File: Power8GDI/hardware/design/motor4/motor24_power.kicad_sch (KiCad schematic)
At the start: 17 parts, among them Q6250 IPD90N10S4-06, Q6251 IPD90N10S4-06, U6250 LM74800QDRRRQ1

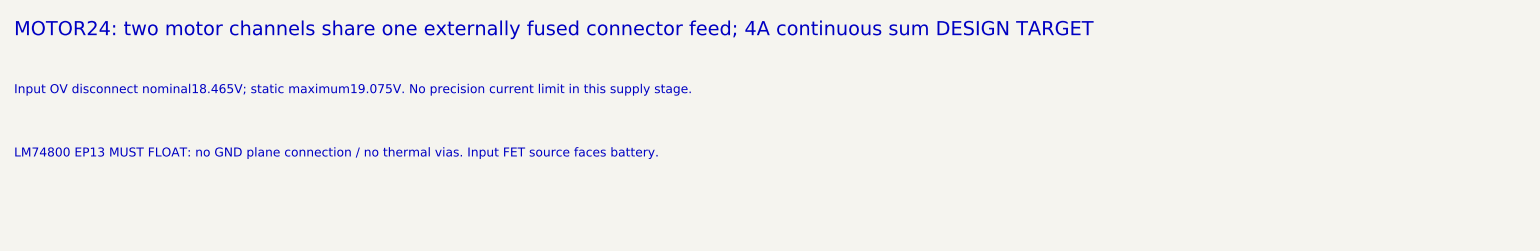
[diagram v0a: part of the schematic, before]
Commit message: Redesign sport target as six DI/PI channels with two motors and one lambda
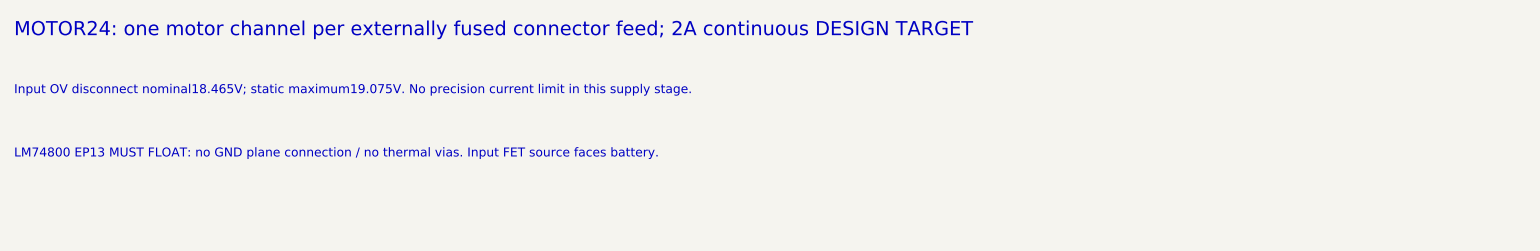
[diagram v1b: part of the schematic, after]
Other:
- note added: "MOTOR24: one motor channel per externally fused connector feed; 2A continuous DESIGN TARGET"
- note removed: "MOTOR24: two motor channels share one externally fused connector feed; 4A continuous sum DESIGN TARGET"
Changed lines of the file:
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@@
 (kicad_sch (version 20250114) (generator "eeschema") (paper "A2") (title_block (title "MOTOR24: independent protected feed") (rev "Engineering draft 0.1") (comment 1 "UNQUALIFIED: no manufacturing or engine approval"))
-(text "MOTOR24: two motor channels share one externally fused connector feed; 4A continuous sum DESIGN TARGET" (at 20 15 0) (effects (font (size 2 2)) (justify left top)))
+(text "MOTOR24: one motor channel per externally fused connector feed; 2A continuous DESIGN TARGET" (at 20 15 0) (effects (font (size 2 2)) (justify left top)))
 (text "Input OV disconnect nominal18.465V; static maximum19.075V. No precision current limit in this supply stage." (at 20 24 0) (effects (font (size 1.27 1.27)) (justify left top)))
 (text "LM74800 EP13 MUST FLOAT: no GND plane connection / no thermal vias. Input FET source faces battery." (at 20 33 0) (effects (font (size 1.27 1.27)) (justify left top)))

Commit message: Review B58 injector power stage and bind selected GDI6 BOM
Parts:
- C6250, C6251, C6252, C6253: Hardware_Qualification (none) -> BOARD_QUALIFICATION_PENDING; MPN (none) -> C0805C104K1RACTU; Manufacturer (none) -> KEMET; Procurement_Status (none) -> SELECTED_CATALOG_ITEM; Purchase_Released (none) -> false; Selection_Gaps (none) -> []; Selection_ID (none) -> SEL-50b208aec5b1; Selection_Ratings (none) -> {"capacitance_pf": 100000, "dielectric": "X7R", "rated_volt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; Selection_Source_URLs (none) -> https://www.mouser.com/datasheet/3/72/1/C0805C104K1RACTU.pdf
- C6254: Hardware_Qualification (none) -> BOARD_QUALIFICATION_PENDING; MPN (none) -> C0805C223K1RACTU; Manufacturer (none) -> KEMET; Procurement_Status (none) -> SELECTED_CATALOG_ITEM; Purchase_Released (none) -> false; Selection_Gaps (none) -> []; Selection_ID (none) -> SEL-514923e6d12b; Selection_Ratings (none) -> {"capacitance_pf": 22000, "dielectric": "X7R", "rated_volta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; Selection_Source_URLs (none) -> https://www.tme.com/Document/1eb495a6db632c9d0f71cb50aeea42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
- D6250: Hardware_Qualification (none) -> PINOUT_RATINGS_AND_DELIVERY_SUFFIX_REVIEW_PENDING; MPN (none) -> SMCJ33CA; Manufacturer (none) -> Littelfuse; Procurement_Status (none) -> REFERENCE_MPN_RETAINED; Purchase_Released (none) -> false; Selection_Gaps (none) -> ["Existing schematic MPN retained. Complete circuit rating/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; Selection_ID (none) -> SEL-57a5ac481027; Selection_Ratings (none) -> {}; Selection_Source_URLs (none) -> https://www.littelfuse.com/products/tvs-diodes/surface-moun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
- Q6250, Q6251: Hardware_Qualification (none) -> PINOUT_RATINGS_AND_DELIVERY_SUFFIX_REVIEW_PENDING; MPN (none) -> IPD90N10S406ATMA1; Manufacturer (none) -> Infineon Technologies; Procurement_Status (none) -> REFERENCE_MPN_RETAINED; Purchase_Released (none) -> false; Selection_Gaps (none) -> ["Existing schematic MPN retained. Complete circuit rating/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; Selection_ID (none) -> SEL-dc1735b932bf; Selection_Ratings (none) -> {}; Selection_Source_URLs (none) -> https://www.infineon.com/part/IPD90N10S4-06
- R6250: Hardware_Qualification (none) -> BOARD_QUALIFICATION_PENDING; MPN (none) -> RG2012P-1403-B-T5; Manufacturer (none) -> Susumu; Procurement_Status (none) -> SELECTED_CATALOG_ITEM; Purchase_Released (none) -> false; Selection_Gaps (none) -> []; Selection_ID (none) -> SEL-aca8c7a4773a; Selection_Ratings (none) -> {"aec_q200": true, "derating": "Use manufacturer power vers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; Selection_Source_URLs (none) -> https://www.digikey.com/en/products/detail/susumu/RG2012P-1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
- R6251: Hardware_Qualification (none) -> BOARD_QUALIFICATION_PENDING; MPN (none) -> RNCF0603BTE10K0; Manufacturer (none) -> Stackpole Electronics; Procurement_Status (none) -> SELECTED_CATALOG_ITEM; Purchase_Released (none) -> false; Selection_Gaps (none) -> []; Selection_ID (none) -> SEL-3a4fba6ce443; Selection_Ratings (none) -> {"aec_q200": true, "derating": "Use manufacturer power vers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; Selection_Source_URLs (none) -> https://www.digikey.com/en/products/detail/stackpole-electr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
- R6252, R6256: Hardware_Qualification (none) -> BOARD_QUALIFICATION_PENDING; MPN (none) -> CRCW06031K00FKEA; Manufacturer (none) -> Vishay; Procurement_Status (none) -> SELECTED_FAMILY_CODE; Purchase_Released (none) -> false; Selection_Gaps (none) -> []; Selection_ID (none) -> SEL-38197231a947; Selection_Ratings (none) -> {"aec_q200": true, "derating": "Use manufacturer power vers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; Selection_Source_URLs (none) -> https://www.vishay.com/docs/20035/dcrcwe3.pdf
- R6253, R6257: Hardware_Qualification (none) -> BOARD_QUALIFICATION_PENDING; MPN (none) -> CRCW060310K0FKEA; Manufacturer (none) -> Vishay; Procurement_Status (none) -> SELECTED_FAMILY_CODE; Purchase_Released (none) -> false; Selection_Gaps (none) -> []; Selection_ID (none) -> SEL-9c0806476875; Selection_Ratings (none) -> {"aec_q200": true, "derating": "Use manufacturer power vers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; Selection_Source_URLs (none) -> https://www.vishay.com/docs/20035/dcrcwe3.pdf
- R6254, R6255: Hardware_Qualification (none) -> BOARD_QUALIFICATION_PENDING; MPN (none) -> CRCW06031M00FKEA; Manufacturer (none) -> Vishay; Procurement_Status (none) -> SELECTED_FAMILY_CODE; Purchase_Released (none) -> false; Selection_Gaps (none) -> []; Selection_ID (none) -> SEL-0d98ae3ae719; Selection_Ratings (none) -> {"aec_q200": true, "derating": "Use manufacturer power vers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; Selection_Source_URLs (none) -> https://www.vishay.com/docs/20035/dcrcwe3.pdf
- U6250: Hardware_Qualification (none) -> BOARD_STRESS_AND_LAYOUT_REVIEW_REQUIRED; MPN (none) -> LM74800QDRRRQ1; Manufacturer (none) -> Texas Instruments; Procurement_Status (none) -> SELECTED_CONDITIONAL; Purchase_Released (none) -> false; Selection_Gaps (none) -> ["Catalog family limits verified; exact order suffix and ci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; Selection_ID (none) -> SEL-9eef1a739cc4; Selection_Ratings (none) -> {"reverse_input_v": -65, "supply_max_v": 65, "supply_min_v"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; Selection_Source_URLs (none) -> https://www.ti.com/product/LM7480-Q1
